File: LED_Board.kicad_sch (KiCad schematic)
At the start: 2 parts, among them J2 Conn_01x02_Pin

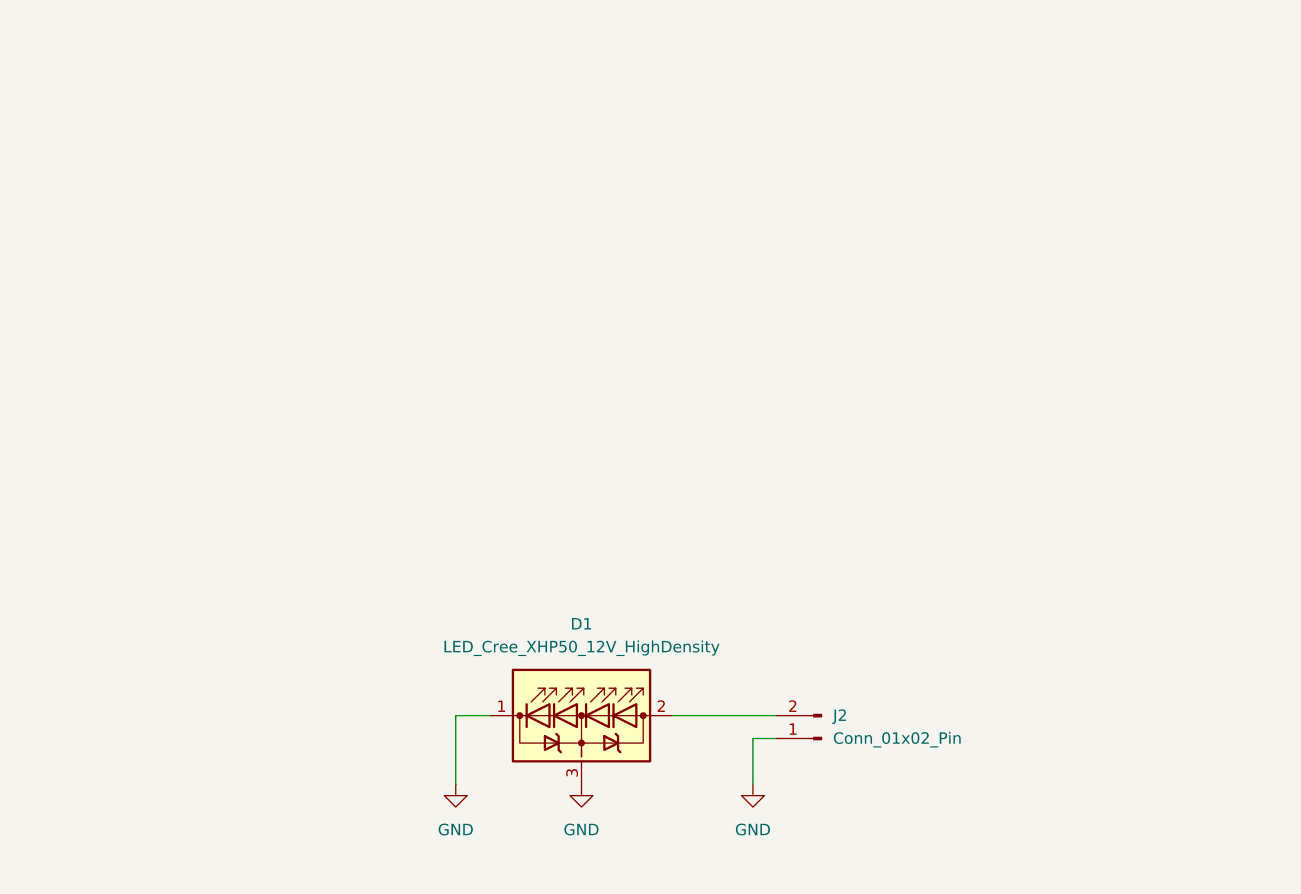
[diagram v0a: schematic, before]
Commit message: Added 6 Warm LEDS and cleanup of silkscreen
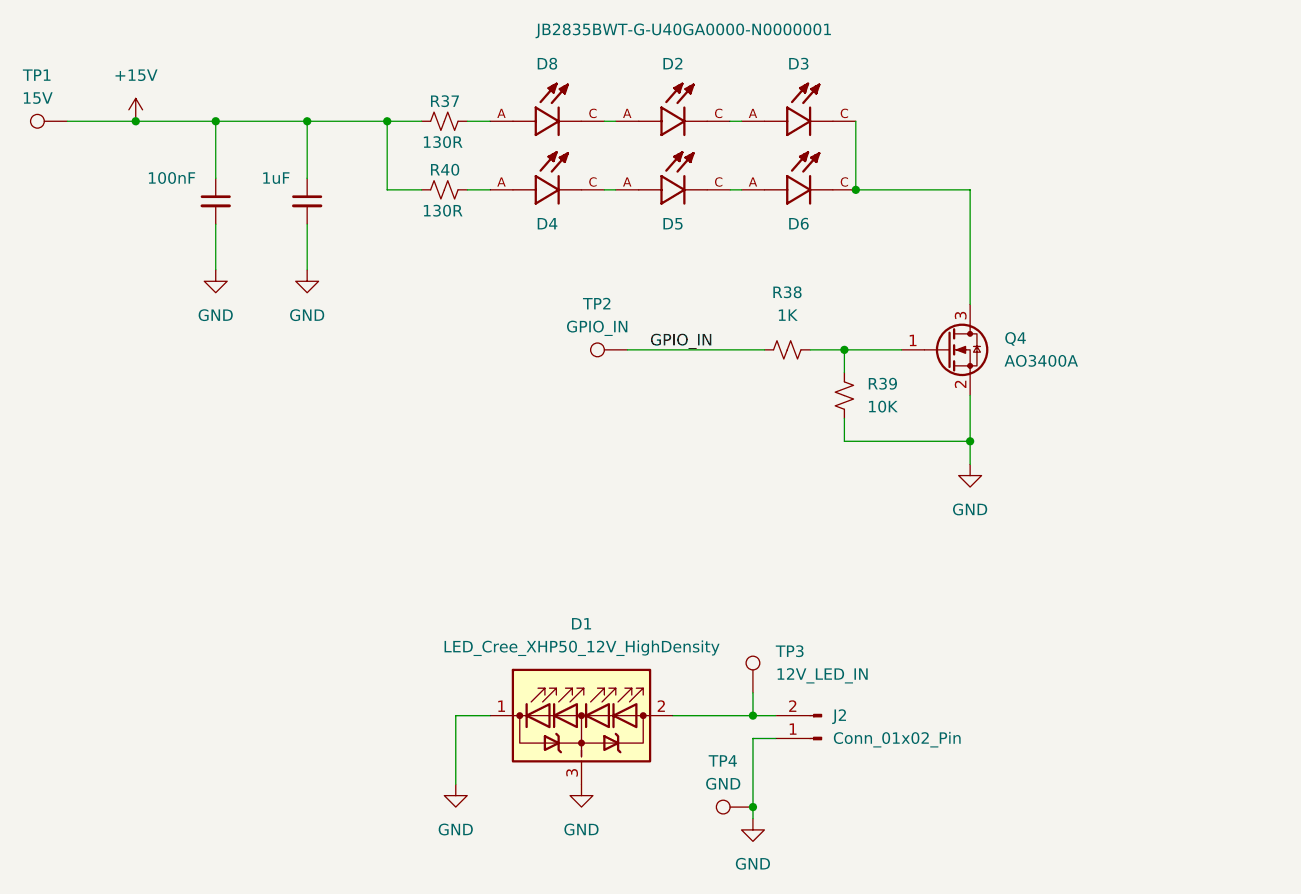
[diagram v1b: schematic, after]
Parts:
- added C1: 100nF, Capacitor_SMD:C_0805_2012Metric, symbol Device:C_Small
- added C2: 1uF, Capacitor_SMD:C_0805_2012Metric, symbol Device:C_Small
- added D2, D3, D4, D5, D6, D8: JB2835BWT-G-U40GA0000-N0000001, Library:LED_JB2835BWT-G-U40GA0000-N0000001, symbol JB2835BWT-G-U40GA0000-N0000001:JB2835BWT-G-U40GA0000-N0000001
- added Q4: AO3400A, Package_TO_SOT_SMD:SOT-23, symbol Transistor_FET:AO3400A
- added R37, R40: 130R, Resistor_SMD:R_0805_2012Metric, symbol Device:R_Small_US
- added R38: 1K, Resistor_SMD:R_0805_2012Metric, symbol Device:R_Small_US
- added R39: 10K, Resistor_SMD:R_0805_2012Metric, symbol Device:R_Small_US
- added TP1: 15V, TestPoint:TestPoint_Pad_2.0x2.0mm, symbol Connector:TestPoint
- added TP2: GPIO_IN, TestPoint:TestPoint_Pad_2.0x2.0mm, symbol Connector:TestPoint
- added TP3: 12V_LED_IN, TestPoint:TestPoint_Pad_2.0x2.0mm, symbol Connector:TestPoint
- added TP4: GND, TestPoint:TestPoint_Pad_2.0x2.0mm, symbol Connector:TestPoint
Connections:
- net GND: now also C1.2, C2.2, Q4.2 (S), R39.1, TP4.1
- net at D1.2 (A), J2.2 (Pin_2): now also TP3.1
- new net: Q4.1 (G), R38.2, R39.2
- new net: D8.A, R37.1
- new net: D2.A, D8.C
- new net: D5.C, D6.A
- new net: D3.C, D6.C, Q4.3 (D)
- new net: D4.C, D5.A
- new net: D2.C, D3.A
- new net: D4.A, R40.1
- new net +15V: C1.1, C2.1, R37.2, R40.2, TP1.1
- new net GPIO_IN: R38.1, TP2.1

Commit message: Added LEDs and fixed V_IN trace widths
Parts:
- added D10: PTVS12VZ1USK, Diode_SMD:Nexperia_DSN1608-2_1.6x0.8mm, symbol Diode:PTVS12VZ1USK
- added D11: PTVS5V0Z1USKP, Diode_SMD:Nexperia_DSN1608-2_1.6x0.8mm, symbol Diode:PTVS5V0Z1USKP
- added D7, D9: JB2835BWT-G-U40GA0000-N0000001, Library:LED_JB2835BWT-G-U40GA0000-N0000001, symbol JB2835BWT-G-U40GA0000-N0000001:JB2835BWT-G-U40GA0000-N0000001
- C1: value 100nF -> 100n
- C2: value 1uF -> 2u2
- R37, R40: value 130R -> 130
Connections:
- net GND: now also D10.2 (A), D11.2 (A)
- net at Q4.1 (G), R38.2, R39.2: now also D11.1 (K)
- new net: D6.C, D9.A
- new net: D3.C, D7.A
- new net: D10.1 (K), D7.C, D9.C, Q4.3 (D)
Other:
- moved on the sheet: R38, R39, TP2

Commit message: Apply all Fixes from Rev 1 (First Pass)
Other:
- note added: "Change to 4 pin or pogos, check the current orientation"
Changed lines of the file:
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@@
 	(generator_version "9.0")
 	(paper "A4")
+	(text "Change to 4 pin or pogos, check the current orientation"
+		(exclude_from_sim no)
+		(at 152.4 118.11 0)
+		(effects
+			(font
+				(size 1.27 1.27)
+			)
+		)
+	)
 	(junction
 		(at 134.62 68.58)

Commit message: Release 1.1.0
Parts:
- removed J2: Conn_01x02_Pin, Connector_Molex:Molex_Micro-Latch_53254-0270_1x02_P2.00mm_Horizontal, symbol Connector:Conn_01x02_Pin
- C1: MPN (none) -> CC0805KRX7R9BB104; URL (none) -> https://www.digikey.com.au/en/products/detail/yageo/CC0805K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
- C2: MPN (none) -> GRM188R61E225KA12D; URL (none) -> https://www.digikey.com.au/en/products/detail/murata-electr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
- D1: MPN (none) -> XHP50D-H0-0000-0D0ZE427G; URL (none) -> https://www.digikey.com.au/en/products/detail/cree-led/XHP5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
- D10: MPN (none) -> PTVS12VZ1USKYL; URL (none) -> https://www.digikey.com.au/en/products/detail/nexperia-usa-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
- D11: MPN (none) -> PTVS5V0Z1USKPYL; URL (none) -> https://www.digikey.com.au/en/products/detail/nexperia-usa-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
- D2, D3, D4, D5, D6, D7, D8, D9: MPN (none) -> JB2835BWT-G-U22GA0000-N0000001; URL (none) -> https://www.digikey.com.au/en/products/detail/cree-led/JB28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
- Q4: MPN (none) -> AO3400A; URL (none) -> https://www.digikey.com.au/en/products/detail/alpha-omega-s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
- R37, R40: MPN (none) -> RMCF0805FT130R; URL (none) -> https://www.digikey.com.au/en/products/detail/stackpole-ele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
- R38: MPN (none) -> RMCF0805FT1K00; URL (none) -> https://www.digikey.com.au/en/products/detail/stackpole-ele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
- R39: MPN (none) -> RMCF0805FT10K0; URL (none) -> https://www.digikey.com.au/en/products/detail/stackpole-ele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
- TP1, TP2, TP3, TP4: now left out of the parts list
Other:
- note removed: "Change to 4 pin or pogos, check the current orientation"
- moved on the sheet: TP4

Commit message: Move
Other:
- note added: "This may be wrong and only use two of the 4 lights"
